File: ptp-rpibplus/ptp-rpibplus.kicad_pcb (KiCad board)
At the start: 2 copper layers, 6 parts, among them J1 RASPI_B+, J2 MODULE_HEADER, J3 MODULE_HEADER

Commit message: better silk for rpi header
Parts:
- J1: footprint Pin_Headers:Pin_Header_Angled_2x20 -> Pin_Headers:Pin_Header_Straight_2x20
- moved J1 10.9 mm to (162.6, 128.3)

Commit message: close to refresh
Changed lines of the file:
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@@
       (effects (font (size 1 1) (thickness 0.1)))
     )
-    (fp_text value MODULE_HEADER (at -13.97 0) (layer F.SilkS)
+    (fp_text value MODULE_HEADER (at -13.97 0) (layer F.SilkS) hide
       (effects (font (size 1 1) (thickness 0.1)))
     )
@@
       (effects (font (size 1 1) (thickness 0.1)))
     )
-    (fp_text value MODULE_HEADER (at -13.97 0) (layer F.SilkS)
+    (fp_text value MODULE_HEADER (at -13.97 0) (layer F.SilkS) hide
       (effects (font (size 1 1) (thickness 0.1)))
     )

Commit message: note about 3.3 rail, updated silk
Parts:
- moved J3 63.9 mm to (102.9, 115.6)
- moved J2 51.9 mm to (207.0, 108.0)

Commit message: drc
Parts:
- moved J3 55.9 mm to (158.8, 113.0)
- moved J2 32.6 mm to (176.5, 119.4)
- moved C3 2.66 mm to (151.1, 105.4)
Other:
- net class Default: clearance 0.254 -> 0.2032; trace_width 0.254 -> 0.2032
- rule trace_clearance: 0.254 -> 0.2032
- rule trace_min: 0.254 -> 0.2032
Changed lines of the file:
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@@
     (links 33)
     (no_connects 33)
-    (area 0 0 0 0)
+    (area 131.49326 101.324156 188.976 131.191001)
     (thickness 1.6)
     (drawings 0)
@@
   )
   (setup
-    (last_trace_width 0.254)
-    (trace_clearance 0.254)
+    (last_trace_width 0.2032)
+    (trace_clearance 0.2032)
     (zone_clearance 0.508)
     (zone_45_only no)
-    (trace_min 0.254)
+    (trace_min 0.2032)
     (segment_width 0.2)
     (edge_width 0.1)
@@
   (net 33 /CLK)
   (net_class Default "This is the default net class."
-    (clearance 0.254)
-    (trace_width 0.254)
+    (clearance 0.2032)
+    (trace_width 0.2032)
     (via_dia 0.889)
     (via_drill 0.635)
@@
   )
   (module Capacitors_SMD:c_0402 (layer F.Cu)
-    (at 148.5011 105.0036)
+    (at 151.13 105.41)
     (descr "SMT capacitor, 0402")
     (fp_text reference C3 (at 0 -0.4826) (layer F.SilkS)
@@
   )
   (module parts:MODULE_HEADER_TESSEL (layer F.Cu)
-    (at 207.01 107.95)
+    (at 176.53 119.38)
     (fp_text reference J2 (at 0 2.54) (layer F.SilkS)
       (effects (font (size 1 1) (thickness 0.1)))
@@
   )
   (module parts:MODULE_HEADER_TESSEL (layer F.Cu)
-    (at 102.87 115.57)
+    (at 158.75 113.03)
     (fp_text reference J3 (at 0 2.54) (layer F.SilkS)
       (effects (font (size 1 1) (thickness 0.1)))

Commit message: ...at least the board has mount holes now
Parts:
- added H1: HOLE, parts:HOLE-2.75mm-6.2mm, F.Cu at (125.7, 102.9)
- added H2: HOLE, parts:HOLE-2.75mm-6.2mm, F.Cu at (137.2, 104.1)
- added H3: HOLE, parts:HOLE-2.75mm-6.2mm, F.Cu at (161.3, 114.3)
- moved J2 50.6 mm to (132.1, 95.2)
- moved C1 29.2 mm to (162.6, 104.1)
- moved J1 23.2 mm to (139.7, 124.5)
- moved J3 21.6 mm to (137.2, 114.3)
- moved C2 18.0 mm to (144.8, 108.0)
- moved C3 2.66 mm to (148.5, 105.0)
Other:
- board outline added: 76.2 x 38.1 mm
- net class Default: clearance 0.2032 -> 0.254; trace_width 0.2032 -> 0.254
- rule trace_clearance: 0.2032 -> 0.254
- rule trace_min: 0.2032 -> 0.254
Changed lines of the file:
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@@
   (general
     (links 33)
-    (no_connects 33)
-    (area 131.49326 101.324156 188.976 131.191001)
+    (no_connects 22)
+    (area 0 0 0 0)
     (thickness 1.6)
-    (drawings 0)
+    (drawings 4)
     (tracks 0)
     (zones 0)
-    (modules 6)
+    (modules 9)
     (nets 34)
   )
@@
   )
   (setup
-    (last_trace_width 0.2032)
-    (trace_clearance 0.2032)
+    (last_trace_width 0.254)
+    (trace_clearance 0.254)
     (zone_clearance 0.508)
     (zone_45_only no)
-    (trace_min 0.2032)
+    (trace_min 0.254)
     (segment_width 0.2)
     (edge_width 0.1)
@@
   (net 33 /CLK)
   (net_class Default "This is the default net class."
-    (clearance 0.2032)
-    (trace_width 0.2032)
+    (clearance 0.254)
+    (trace_width 0.254)
     (via_dia 0.889)
     (via_drill 0.635)
@@
   )
   (module Capacitors_SMD:c_0805 (layer F.Cu)
-    (at 133.35 102.87)
+    (at 162.56 104.14)
     (descr "SMT capacitor, 0805")
     (fp_text reference C1 (at 0 -0.9906) (layer F.SilkS)
@@
   )
   (module Capacitors_SMD:c_0402 (layer F.Cu)
-    (at 162.56 105.41)
+    (at 144.78 107.95)
     (descr "SMT capacitor, 0402")
     (fp_text reference C2 (at 0 -0.4826) (layer F.SilkS)
@@
   )
   (module Capacitors_SMD:c_0402 (layer F.Cu)
-    (at 151.13 105.41)
+    (at 148.5011 105.0036)
     (descr "SMT capacitor, 0402")
     (fp_text reference C3 (at 0 -0.4826) (layer F.SilkS)
@@
     )
   )
+  (module parts:HOLE-2.75mm-6.2mm (layer F.Cu)
+    (at 125.73 102.87)
+    (fp_text reference H1 (at 0 -5.08) (layer F.SilkS) hide
+      (effects (font (size 1 1) (thickness 0.15)))
+    )
+    (fp_text value HOLE (at 0 5.08) (layer F.SilkS) hide
+      (effects (font (size 1 1) (thickness 0.15)))
+    )
+    (pad "" np_thru_hole circle (at 0 0) (size 6.2 6.2) (drill 2.75) (layers *.Cu *.Mask F.SilkS))
+  )
+  (module parts:HOLE-2.75mm-6.2mm (layer F.Cu)
+    (at 137.16 104.14)
+    (fp_text reference H2 (at 0 -5.08) (layer F.SilkS) hide
+      (effects (font (size 1 1) (thickness 0.15)))
+    )
+    (fp_text value HOLE (at 0 5.08) (layer F.SilkS) hide
+      (effects (font (size 1 1) (thickness 0.15)))
+    )
+    (pad "" np_thru_hole circle (at 0 0) (size 6.2 6.2) (drill 2.75) (layers *.Cu *.Mask F.SilkS))
+  )
+  (module parts:HOLE-2.75mm-6.2mm (layer F.Cu)
+    (at 161.29 114.3)
+    (fp_text reference H3 (at 0 -5.08) (layer F.SilkS) hide
+      (effects (font (size 1 1) (thickness 0.15)))
+    )
+    (fp_text value HOLE (at 0 5.08) (layer F.SilkS) hide
+      (effects (font (size 1 1) (thickness 0.15)))
+    )
+    (pad "" np_thru_hole circle (at 0 0) (size 6.2 6.2) (drill 2.75) (layers *.Cu *.Mask F.SilkS))
+  )
   (module Pin_Headers:Pin_Header_Straight_2x20 (layer F.Cu)
-    (at 162.56 128.27)
+    (at 139.7 124.46)
     (descr "1 pin")
     (tags "CONN DEV")
@@
   )
   (module parts:MODULE_HEADER_TESSEL (layer F.Cu)
-    (at 176.53 119.38)
+    (at 132.08 95.25)
     (fp_text reference J2 (at 0 2.54) (layer F.SilkS)
       (effects (font (size 1 1) (thickness 0.1)))
@@
   )
   (module parts:MODULE_HEADER_TESSEL (layer F.Cu)
-    (at 158.75 113.03)
+    (at 137.16 114.3)
     (fp_text reference J3 (at 0 2.54) (layer F.SilkS)
       (effects (font (size 1 1) (thickness 0.1)))
@@
       (net 13 /B_G3))
   )
+  (gr_line (start 101.6 88.9) (end 101.6 127) (layer Edge.Cuts) (width 0.2))
+  (gr_line (start 177.8 88.9) (end 101.6 88.9) (layer Edge.Cuts) (width 0.2))
+  (gr_line (start 177.8 127) (end 177.8 88.9) (layer Edge.Cuts) (width 0.2))
+  (gr_line (start 101.6 127) (end 177.8 127) (layer Edge.Cuts) (width 0.2))
 )

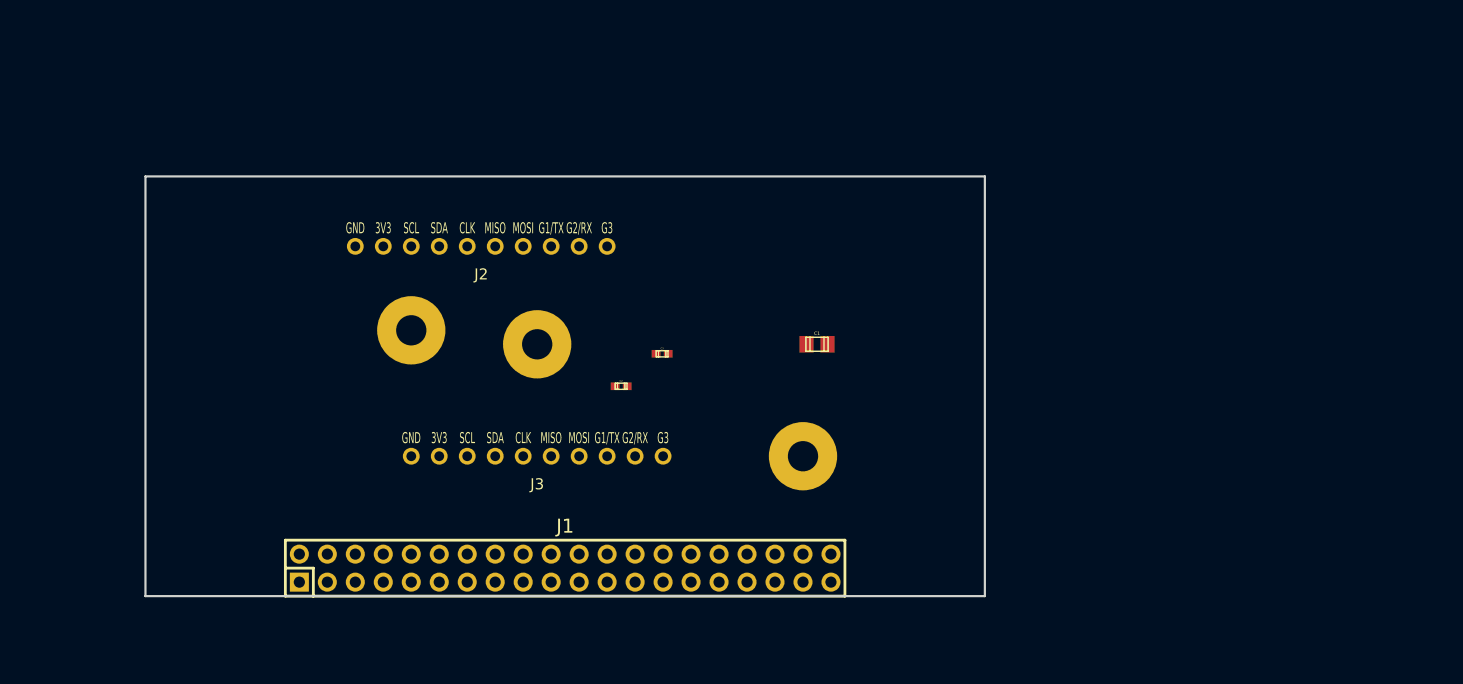
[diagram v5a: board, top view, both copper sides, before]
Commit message: how did the pcb files not get added?
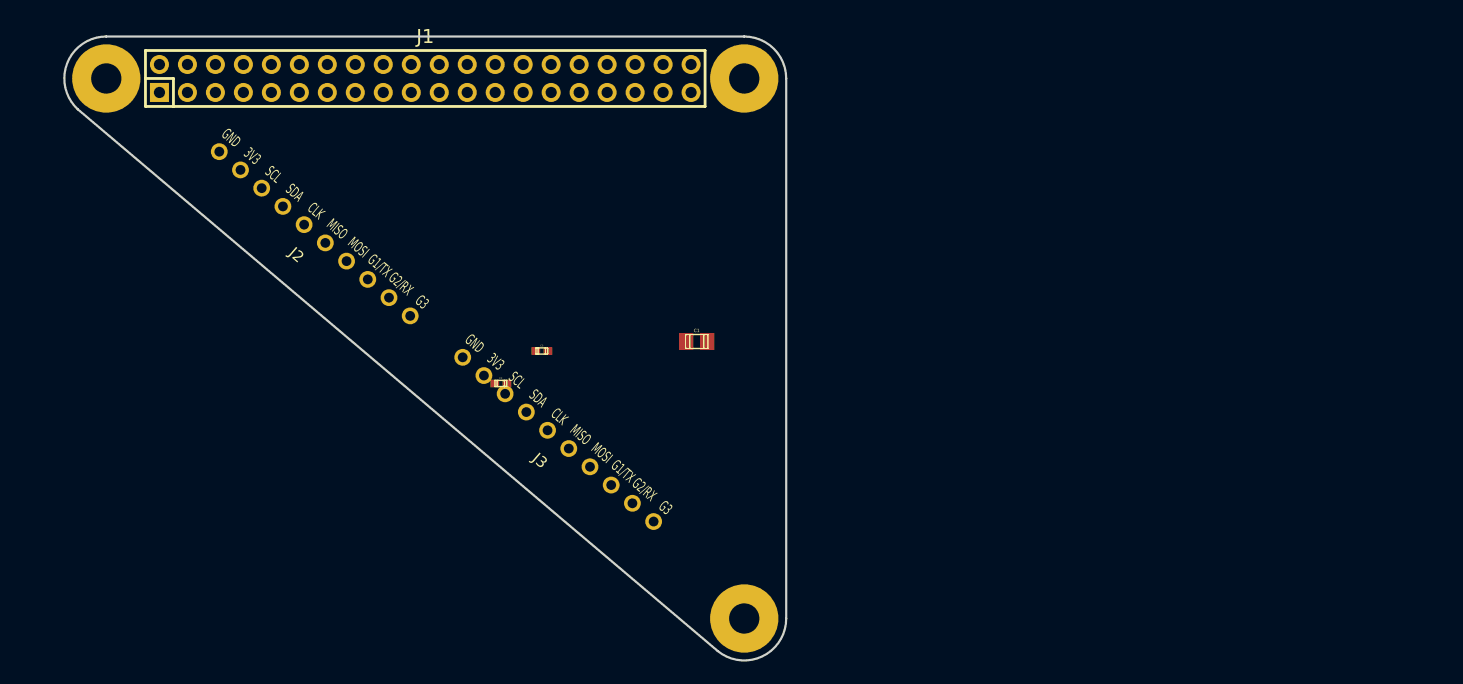
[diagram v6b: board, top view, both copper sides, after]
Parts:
- moved J1 46.2 mm to (127.0, 80.0)
- moved H1 35.9 mm to (98.0, 80.0), turned to 90 degrees
- moved H3 34.7 mm to (156.2, 80.0)
- moved H2 31.2 mm to (156.0, 129.0)
- moved J2 15.2 mm to (117.0, 94.1), turned to 319.3 degrees
- moved C1 10.9 mm to (151.6, 103.9)
- moved C2 10.9 mm to (133.9, 107.7)
- moved C3 10.9 mm to (137.6, 104.7)
- moved J3 2.44 mm to (139.1, 112.8), turned to 319.3 degrees
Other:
- board size 76.2 x 38.1 mm -> 65.5 x 56.6 mm

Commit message: positioning things is hard
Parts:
- moved C2 19.1 mm to (149.9, 97.3)
- moved C1 15.8 mm to (144.8, 89.7)
- moved C3 13.3 mm to (137.7, 91.4)
- moved J3 6.88 mm to (145.9, 112.2), turned to 319.8 degrees
- moved J2 5.84 mm to (122.6, 92.6), turned to 319.8 degrees

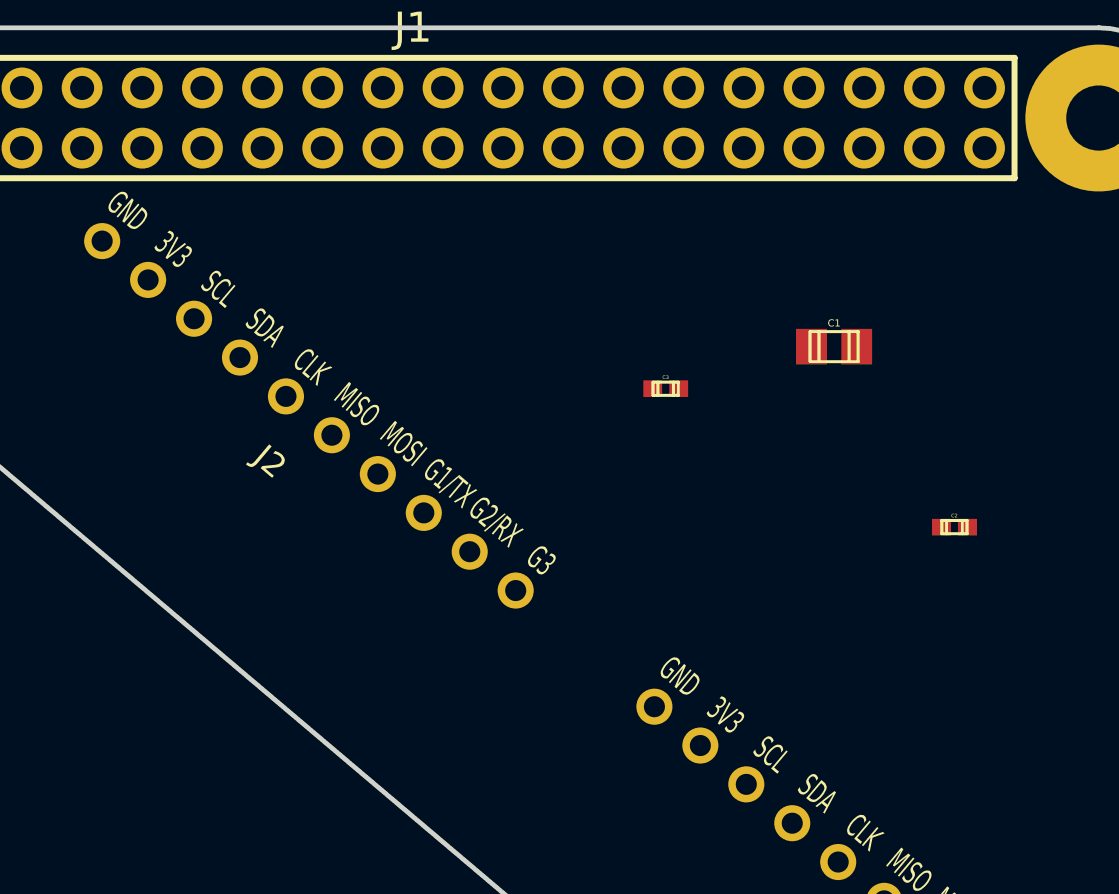
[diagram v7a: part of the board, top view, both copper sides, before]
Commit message: started routing, decided to pursue parallel instead
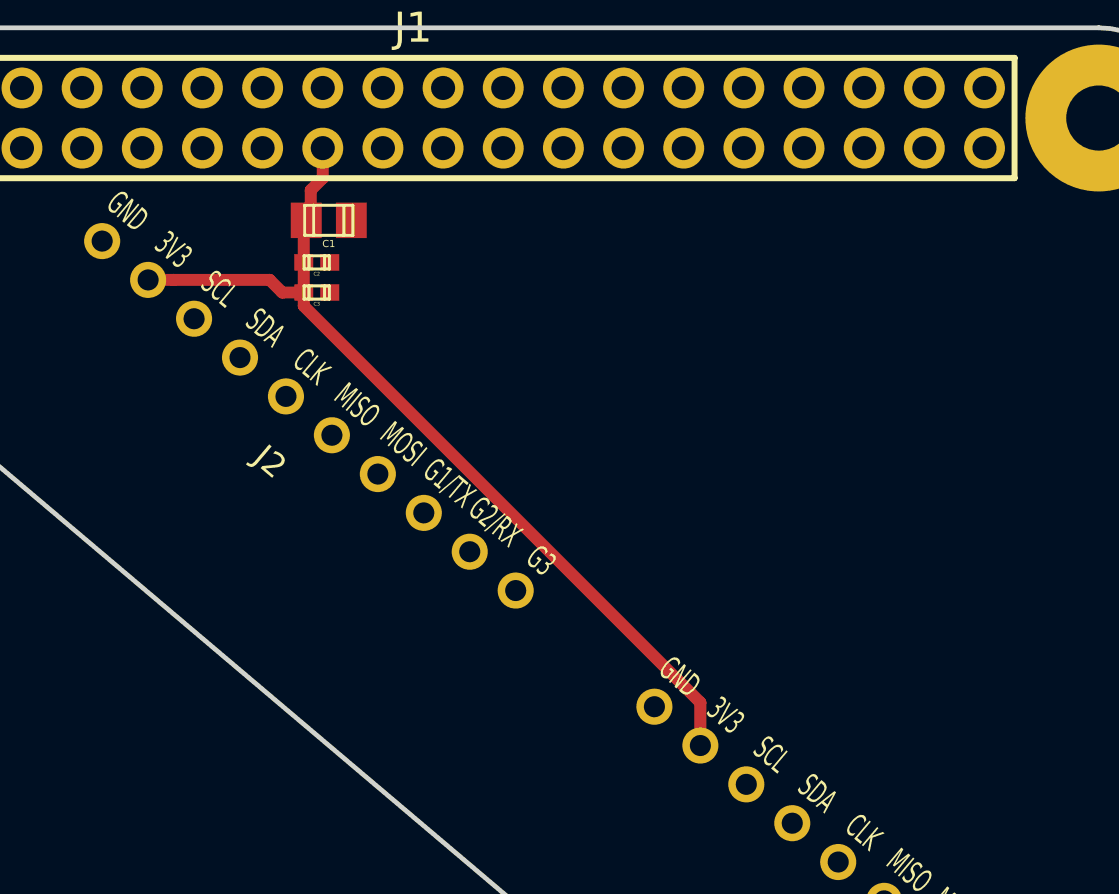
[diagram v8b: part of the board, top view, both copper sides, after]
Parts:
- moved C2 29.2 mm to (122.9, 86.1), turned to 180 degrees
- moved C1 22.0 mm to (123.4, 84.3), turned to 180 degrees
- moved C3 15.3 mm to (122.9, 87.4), turned to 180 degrees
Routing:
- net 3V3: track 0.00 -> 39.3 mm
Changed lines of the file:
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@@
     (thickness 1.6)
     (drawings 11)
-    (tracks 0)
+    (tracks 14)
     (zones 0)
     (modules 9)
@@
   )
   (setup
-    (last_trace_width 0.254)
+    (last_trace_width 0.508)
     (trace_clearance 0.254)
     (zone_clearance 0.508)
@@
   )
   (module Capacitors_SMD:c_0805 (layer F.Cu)
-    (at 144.78 89.662)
+    (at 123.444 84.328 180)
     (descr "SMT capacitor, 0805")
-    (fp_text reference C1 (at 0 -0.9906) (layer F.SilkS)
+    (fp_text reference C1 (at 0 -0.9906 180) (layer F.SilkS)
       (effects (font (size 0.29972 0.29972) (thickness 0.06096)))
     )
-    (fp_text value 10uF (at 0 0.9906) (layer F.SilkS) hide
+    (fp_text value 10uF (at 0 0.9906 180) (layer F.SilkS) hide
       (effects (font (size 0.29972 0.29972) (thickness 0.06096)))
     )
@@
     (fp_line (start 1.016 0.635) (end -1.016 0.635) (layer F.SilkS) (width 0.127))
     (fp_line (start -1.016 0.635) (end -1.016 -0.635) (layer F.SilkS) (width 0.127))
-    (pad 1 smd rect (at 0.9525 0) (size 1.30048 1.4986) (layers F.Cu F.Paste F.Mask)
-      (net 1 3V3))
-    (pad 2 smd rect (at -0.9525 0) (size 1.30048 1.4986) (layers F.Cu F.Paste F.Mask)
+    (pad 1 smd rect (at 0.9525 0 180) (size 1.30048 1.4986) (layers F.Cu F.Paste F.Mask)
+      (net 1 3V3))
+    (pad 2 smd rect (at -0.9525 0 180) (size 1.30048 1.4986) (layers F.Cu F.Paste F.Mask)
       (net 2 GND))
     (model smd/Capacitors/C0805.wrl
@@
   )
   (module Capacitors_SMD:c_0402 (layer F.Cu)
-    (at 149.86 97.282)
+    (at 122.936 86.106 180)
     (descr "SMT capacitor, 0402")
-    (fp_text reference C2 (at 0 -0.4826) (layer F.SilkS)
+    (fp_text reference C2 (at 0 -0.4826 180) (layer F.SilkS)
       (effects (font (size 0.1524 0.1524) (thickness 0.03048)))
     )
-    (fp_text value 1uF (at 0 0.4826) (layer F.SilkS) hide
+    (fp_text value 1uF (at 0 0.4826 180) (layer F.SilkS) hide
       (effects (font (size 0.1524 0.1524) (thickness 0.03048)))
     )
@@
     (fp_line (start 0.5334 0.2794) (end 0.5334 -0.2794) (layer F.SilkS) (width 0.127))
     (fp_line (start 0.5334 -0.2794) (end -0.5334 -0.2794) (layer F.SilkS) (width 0.127))
-    (pad 1 smd rect (at 0.54864 0) (size 0.8001 0.6985) (layers F.Cu F.Paste F.Mask)
-      (net 1 3V3))
-    (pad 2 smd rect (at -0.54864 0) (size 0.8001 0.6985) (layers F.Cu F.Paste F.Mask)
+    (pad 1 smd rect (at 0.54864 0 180) (size 0.8001 0.6985) (layers F.Cu F.Paste F.Mask)
+      (net 1 3V3))
+    (pad 2 smd rect (at -0.54864 0 180) (size 0.8001 0.6985) (layers F.Cu F.Paste F.Mask)
       (net 2 GND))
     (model smd/capacitors/c_0402.wrl
@@
   )
   (module Capacitors_SMD:c_0402 (layer F.Cu)
-    (at 137.668 91.44)
+    (at 122.936 87.376 180)
     (descr "SMT capacitor, 0402")
-    (fp_text reference C3 (at 0 -0.4826) (layer F.SilkS)
+    (fp_text reference C3 (at 0 -0.4826 180) (layer F.SilkS)
       (effects (font (size 0.1524 0.1524) (thickness 0.03048)))
     )
-    (fp_text value 100nF (at 0 0.4826) (layer F.SilkS) hide
+    (fp_text value 100nF (at 0 0.4826 180) (layer F.SilkS) hide
       (effects (font (size 0.1524 0.1524) (thickness 0.03048)))
     )
@@
     (fp_line (start 0.5334 0.2794) (end 0.5334 -0.2794) (layer F.SilkS) (width 0.127))
     (fp_line (start 0.5334 -0.2794) (end -0.5334 -0.2794) (layer F.SilkS) (width 0.127))
-    (pad 1 smd rect (at 0.54864 0) (size 0.8001 0.6985) (layers F.Cu F.Paste F.Mask)
-      (net 1 3V3))
-    (pad 2 smd rect (at -0.54864 0) (size 0.8001 0.6985) (layers F.Cu F.Paste F.Mask)
+    (pad 1 smd rect (at 0.54864 0 180) (size 0.8001 0.6985) (layers F.Cu F.Paste F.Mask)
+      (net 1 3V3))
+    (pad 2 smd rect (at -0.54864 0 180) (size 0.8001 0.6985) (layers F.Cu F.Paste F.Mask)
       (net 2 GND))
     (model smd/capacitors/c_0402.wrl
@@
     (arrow2b (pts (xy 98.044 66.04) (xy 99.170504 65.453579)))
   )
+  (segment (start 139.132853 106.504481) (end 139.132853 104.687915) (width 0.508) (layer F.Cu) (net 1))
+  (segment (start 139.132853 104.687915) (end 122.38736 87.942422) (width 0.508) (layer F.Cu) (net 1))
+  (segment (start 122.38736 87.942422) (end 122.38736 87.376) (width 0.508) (layer F.Cu) (net 1))
+  (segment (start 122.38736 87.376) (end 121.47931 87.376) (width 0.508) (layer F.Cu) (net 1))
+  (segment (start 121.47931 87.376) (end 120.948191 86.844881) (width 0.508) (layer F.Cu) (net 1))
+  (segment (start 120.948191 86.844881) (end 116.893283 86.844881) (width 0.508) (layer F.Cu) (net 1))
+  (segment (start 116.893283 86.844881) (end 115.815653 86.844881) (width 0.508) (layer F.Cu) (net 1))
+  (segment (start 122.38736 87.376) (end 122.38736 86.106) (width 0.508) (layer F.Cu) (net 1))
+  (segment (start 122.38736 86.106) (end 122.38736 84.43214) (width 0.508) (layer F.Cu) (net 1))
+  (segment (start 122.38736 84.43214) (end 122.4915 84.328) (width 0.508) (layer F.Cu) (net 1))
+  (segment (start 123.19 81.28) (end 123.19 82.55) (width 0.508) (layer F.Cu) (net 1))
+  (segment (start 123.19 82.55) (end 122.682 83.058) (width 0.508) (layer F.Cu) (net 1))
+  (segment (start 122.682 83.058) (end 122.682 84.1375) (width 0.508) (layer F.Cu) (net 1))
+  (segment (start 122.682 84.1375) (end 122.4915 84.328) (width 0.508) (layer F.Cu) (net 1))
 )
